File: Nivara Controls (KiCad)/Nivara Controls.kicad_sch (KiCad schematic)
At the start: 11 parts, among them J1 Screw_Terminal_2_P5.00mm, J10 Screw_Terminal_6_P5.00mm, J2 Screw_Terminal_2_P5.00mm, J3 Screw_Terminal_2_P5.00mm, J4 Screw_Terminal_4_P5.00mm, J5 Screw_Terminal_2_P5.00mm, J6 Screw_Terminal_2_P5.00mm, J7 Screw_Terminal_3_P5.00mm, J8 Screw_Terminal_3_P5.00mm, J9 Screw_Terminal_4_P5.00mm

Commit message: Actualization
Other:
- moved on the sheet: J5
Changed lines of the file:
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@@
 	(wire
 		(pts
-			(xy 138.43 142.24) (xy 143.51 142.24)
+			(xy 139.7 142.24) (xy 143.51 142.24)
 		)
 		(stroke
@@
 	(wire
 		(pts
-			(xy 138.43 144.78) (xy 143.51 144.78)
+			(xy 139.7 144.78) (xy 143.51 144.78)
 		)
 		(stroke
@@
 	(symbol
 		(lib_id "PCM_SL_Screw_Terminal:Screw_Terminal_2_P5.00mm")
-		(at 134.62 143.51 180)
+		(at 135.89 143.51 180)
 		(unit 1)
 		(exclude_from_sim no)
@@
 		(dnp no)
 		(property "Reference" "J5"
-			(at 129.794 144.018 0)
+			(at 131.064 144.018 0)
 			(effects
 				(font
@@
 		)
 		(property "Value" "Screw_Terminal_2_P5.00mm"
-			(at 133.985 138.43 0)
+			(at 135.255 138.43 0)
 			(effects
 				(font
@@
 		)
 		(property "Footprint" "TerminalBlock_Phoenix:TerminalBlock_Phoenix_PT-1,5-2-5.0-H_1x02_P5.00mm_Horizontal"
-			(at 133.35 137.16 0)
+			(at 134.62 137.16 0)
 			(effects
 				(font
@@
 		)
 		(property "Datasheet" ""
-			(at 134.62 143.51 0)
+			(at 135.89 143.51 0)
 			(effects
 				(font
@@
 		)
 		(property "Description" ""
-			(at 134.62 143.51 0)
+			(at 135.89 143.51 0)
 			(effects
 				(font
@@
 		)
 		(property "Part Number" ""
-			(at 134.62 143.51 0)
-			(effects
-				(font
+			(at 135.89 143.51 0)
+			(effects
+				(font

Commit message: Actualización
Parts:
- removed J5: Screw_Terminal_2_P5.00mm, TerminalBlock_Phoenix:TerminalBlock_Phoenix_PT-1,5-2-5.0-H_1x02_P5.00mm_Horizontal, symbol PCM_SL_Screw_Terminal:Screw_Terminal_2_P5.00mm
- added J5: Screw_Terminal_4_P5.00mm, TerminalBlock_Phoenix:TerminalBlock_Phoenix_PT-1,5-4-5.0-H_1x04_P5.00mm_Horizontal, symbol PCM_SL_Screw_Terminal:Screw_Terminal_4_P5.00mm
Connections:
- new net Board_NIVARA/+Digit_input_1_+: J5.1
- new net Board_NIVARA/+Digit_input_2_+: J5.3
- new net Board_NIVARA/-Digit_input_1_-: J5.2
- new net Board_NIVARA/-Digit_input_2_-: J5.4
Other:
- sheet Board_NIVARA ports: added +Digit_input_1_+, +Digit_input_2_+, -Digit_input_1_-, -Digit_input_2_-; removed Digit_input_1, Digit_input_2
- moved on the sheet: J1
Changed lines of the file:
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@@
 	(text "24V DC\n"
 		(exclude_from_sim no)
-		(at 124.714 77.978 0)
+		(at 138.684 83.058 0)
 		(effects
 			(font
@@
 	(wire
 		(pts
+			(xy 139.7 140.97) (xy 143.51 140.97)
+		)
+		(stroke
+			(width 0)
+			(type default)
+		)
+	)
+	(wire
+		(pts
 			(xy 201.93 101.6) (xy 205.74 101.6)
 		)
@@
 	(wire
 		(pts
-			(xy 139.7 142.24) (xy 143.51 142.24)
-		)
-		(stroke
-			(width 0)
-			(type default)
-		)
-	)
-	(wire
-		(pts
 			(xy 139.7 120.65) (xy 143.51 120.65)
 		)
@@
 	(wire
 		(pts
+			(xy 139.7 143.51) (xy 143.51 143.51)
+		)
+		(stroke
+			(width 0)
+			(type default)
+		)
+	)
+	(wire
+		(pts
 			(xy 140.97 128.27) (xy 140.97 129.54)
 		)
@@
 	(wire
 		(pts
-			(xy 139.7 144.78) (xy 143.51 144.78)
-		)
-		(stroke
-			(width 0)
-			(type default)
-		)
-	)
-	(wire
-		(pts
 			(xy 139.7 113.03) (xy 143.51 113.03)
 		)
@@
 	(wire
 		(pts
-			(xy 116.84 78.74) (xy 120.65 78.74)
+			(xy 130.81 83.82) (xy 134.62 83.82)
 		)
 		(stroke
@@
 	(wire
 		(pts
-			(xy 120.65 78.74) (xy 120.65 82.55)
+			(xy 134.62 83.82) (xy 134.62 87.63)
+		)
+		(stroke
+			(width 0)
+			(type default)
+		)
+	)
+	(wire
+		(pts
+			(xy 139.7 138.43) (xy 143.51 138.43)
 		)
 		(stroke
@@
 	(wire
 		(pts
+			(xy 139.7 146.05) (xy 143.51 146.05)
+		)
+		(stroke
+			(width 0)
+			(type default)
+		)
+	)
+	(wire
+		(pts
 			(xy 140.97 154.94) (xy 139.7 154.94)
 		)
@@
 	(wire
 		(pts
-			(xy 116.84 76.2) (xy 120.65 76.2)
-		)
-		(stroke
-			(width 0)
-			(type default)
-		)
-	)
-	(wire
-		(pts
-			(xy 120.65 76.2) (xy 120.65 73.66)
+			(xy 130.81 81.28) (xy 134.62 81.28)
+		)
+		(stroke
+			(width 0)
+			(type default)
+		)
+	)
+	(wire
+		(pts
+			(xy 134.62 81.28) (xy 134.62 78.74)
 		)
 		(stroke
@@
 	(symbol
 		(lib_id "power:GND")
-		(at 120.65 82.55 0)
+		(at 134.62 87.63 0)
 		(unit 1)
 		(exclude_from_sim no)
@@
 		(dnp no)
 		(property "Reference" "#PWR01"
-			(at 120.65 88.9 0)
+			(at 134.62 93.98 0)
 			(effects
 				(font
@@
 		)
 		(property "Value" "GND"
-			(at 120.65 86.614 0)
+			(at 134.62 91.694 0)
 			(effects
 				(font
@@
 		)
 		(property "Footprint" ""
-			(at 120.65 82.55 0)
+			(at 134.62 87.63 0)
 			(effects
 				(font
@@
 		)
 		(property "Datasheet" ""
-			(at 120.65 82.55 0)
+			(at 134.62 87.63 0)
 			(effects
 				(font
@@
 		)
 		(property "Description" "Power symbol creates a global label with name \"GND\" , ground"
-			(at 120.65 82.55 0)
+			(at 134.62 87.63 0)
 			(effects
 				(font
@@
 				(path "/42622735-4343-4315-af64-a45701a752b6"
 					(reference "#PWR01")
-					(unit 1)
-				)
-			)
-		)
-	)
-	(symbol
-		(lib_id "PCM_SL_Screw_Terminal:Screw_Terminal_2_P5.00mm")
-		(at 135.89 143.51 180)
-		(unit 1)
-		(exclude_from_sim no)
-		(in_bom yes)
-		(on_board yes)
-		(dnp no)
-		(property "Reference" "J5"
-			(at 131.064 144.018 0)
-			(effects
-				(font
-					(size 1.27 1.27)
-				)
-			)
-		)
-		(property "Value" "Screw_Terminal_2_P5.00mm"
-			(at 135.255 138.43 0)
-			(effects
-				(font
-					(size 1.27 1.27)
-				)
-				(hide yes)
-			)
-		)
-		(property "Footprint" "TerminalBlock_Phoenix:TerminalBlock_Phoenix_PT-1,5-2-5.0-H_1x02_P5.00mm_Horizontal"
-			(at 134.62 137.16 0)
-			(effects
-				(font
-					(size 1.27 1.27)
-				)
-				(hide yes)
-			)
-		)
-		(property "Datasheet" ""
-			(at 135.89 143.51 0)
-			(effects
-				(font
-					(size 1.27 1.27)
-				)
-				(hide yes)
-			)
-		)
-		(property "Description" ""
-			(at 135.89 143.51 0)
-			(effects
-				(font
-					(size 1.27 1.27)
-				)
-				(hide yes)
-			)
-		)
-		(property "Part Number" ""
-			(at 135.89 143.51 0)
-			(effects
-				(font
-					(size 1.27 1.27)
-				)
-			)
-		)
-		(pin "1"
-		)
-		(pin "2"
-		)
-		(instances
-			(project "Nivara Controls"
-				(path "/42622735-4343-4315-af64-a45701a752b6"
-					(reference "J5")
 					(unit 1)
 				)
@@
 	(symbol
 		(lib_id "power:VCC")
-		(at 120.65 73.66 0)
+		(at 134.62 78.74 0)
 		(unit 1)
 		(exclude_from_sim no)
@@
 		(dnp no)
 		(property "Reference" "#PWR02"
-			(at 120.65 77.47 0)
+			(at 134.62 82.55 0)
 			(effects
 				(font
@@
 		)
 		(property "Value" "VCC"
-			(at 120.65 69.85 0)
+			(at 134.62 74.93 0)
 			(effects
 				(font
@@
 		)
 		(property "Footprint" ""
-			(at 120.65 73.66 0)
+			(at 134.62 78.74 0)
 			(effects
 				(font
@@
 		)
 		(property "Datasheet" ""
-			(at 120.65 73.66 0)
+			(at 134.62 78.74 0)
 			(effects
 				(font
@@
 		)
 		(property "Description" "Power symbol creates a global label with name \"VCC\""
-			(at 120.65 73.66 0)
+			(at 134.62 78.74 0)
 			(effects
 				(font
@@
 	)
 	(symbol
+		(lib_id "PCM_SL_Screw_Terminal:Screw_Terminal_4_P5.00mm")
+		(at 135.89 142.24 0)
+		(mirror y)
+		(unit 1)
+		(exclude_from_sim no)
+		(in_bom yes)
+		(on_board yes)
+		(dnp no)
+		(property "Reference" "J5"
+			(at 132.08 140.9699 0)
+			(effects
+				(font
+					(size 1.27 1.27)
+				)
+				(justify left)
+			)
+		)
+		(property "Value" "Screw_Terminal_4_P5.00mm"
+			(at 132.08 143.5099 0)
+			(effects
+				(font
+					(size 1.27 1.27)
+				)
+				(justify left)
+				(hide yes)
+			)
+		)
+		(property "Footprint" "TerminalBlock_Phoenix:TerminalBlock_Phoenix_PT-1,5-4-5.0-H_1x04_P5.00mm_Horizontal"
+			(at 135.89 151.13 0)
+			(effects
+				(font
+					(size 1.27 1.27)
+				)
+				(hide yes)
+			)
+		)
+		(property "Datasheet" ""
+			(at 135.89 139.7 0)
+			(effects
+				(font
+					(size 1.27 1.27)
+				)
+				(hide yes)
+			)
+		)
+		(property "Description" ""
+			(at 135.89 142.24 0)
+			(effects
+				(font
+					(size 1.27 1.27)
+				)
+				(hide yes)
+			)
+		)
+		(property "Part Number" ""
+			(at 135.89 142.24 0)
+			(effects
+				(font
+					(size 1.27 1.27)
+				)
+			)
+		)
+		(pin "3"
+		)
+		(pin "2"
+		)
+		(pin "1"
+		)
+		(pin "4"
+		)
+		(instances
+			(project "Nivara Controls"
+				(path "/42622735-4343-4315-af64-a45701a752b6"
+					(reference "J5")
+					(unit 1)
+				)
+			)
+		)
+	)
+	(symbol
 		(lib_id "PCM_SL_Screw_Terminal:Screw_Terminal_2_P5.00mm")
-		(at 113.03 77.47 180)
+		(at 127 82.55 180)
 		(unit 1)
 		(exclude_from_sim no)
@@
 		(dnp no)
 		(property "Reference" "J1"
-			(at 108.204 77.978 0)
+			(at 122.174 83.058 0)
 			(effects
 				(font
@@
 		)
 		(property "Value" "Screw_Terminal_2_P5.00mm"
-			(at 112.395 72.39 0)
+			(at 126.365 77.47 0)
 			(effects
 				(font
@@
 		)
 		(property "Footprint" "TerminalBlock_Phoenix:TerminalBlock_Phoenix_PT-1,5-2-5.0-H_1x02_P5.00mm_Horizontal"
-			(at 111.76 71.12 0)
+			(at 125.73 76.2 0)
 			(effects
 				(font
@@
 		)
 		(property "Datasheet" ""
-			(at 113.03 77.47 0)
+			(at 127 82.55 0)
 			(effects
 				(font
@@
 		)
 		(property "Description" ""
-			(at 113.03 77.47 0)
+			(at 127 82.55 0)
 			(effects
 				(font
@@
 		)
 		(property "Part Number" ""
-			(at 113.03 77.47 0)
+			(at 127 82.55 0)
 			(effects
 				(font
@@
 			)
 		)
-		(pin "Digit_input_1" input
-			(at 143.51 142.24 180)
-			(effects
-				(font
-					(size 1.27 1.27)
-				)
-				(justify left)
-			)
-		)
-		(pin "Digit_input_2" input
-			(at 143.51 144.78 180)
-			(effects
-				(font
-					(size 1.27 1.27)
-				)
-				(justify left)
-			)
-		)
 		(pin "NPN_input_1" input
 			(at 143.51 100.33 180)
@@
 			)
 		)
+		(pin "+Digit_input_1_+" input
+			(at 143.51 138.43 180)
+			(effects
+				(font
+					(size 1.27 1.27)
+				)
+				(justify left)
+			)
+		)
+		(pin "+Digit_input_2_+" input
+			(at 143.51 143.51 180)
+			(effects
+				(font
+					(size 1.27 1.27)
+				)
+				(justify left)
+			)
+		)
+		(pin "-Digit_input_1_-" input
+			(at 143.51 140.97 180)
+			(effects
+				(font
+					(size 1.27 1.27)
+				)
+				(justify left)
+			)
+		)
+		(pin "-Digit_input_2_-" input
+			(at 143.51 146.05 180)
+			(effects
+				(font
+					(size 1.27 1.27)
+				)
+				(justify left)
+			)
+		)

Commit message: Trabajando en PCB
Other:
- moved on the sheet: J1
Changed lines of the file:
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@@
+	(wire
+		(pts
+			(xy 127 81.28) (xy 134.62 81.28)
+		)
+		(stroke
+			(width 0)
+			(type default)
+		)
+	)
 	(wire
 		(pts
@@
 	(wire
 		(pts
-			(xy 130.81 83.82) (xy 134.62 83.82)
-		)
-		(stroke
-			(width 0)
-			(type default)
-		)
-	)
-	(wire
-		(pts
 			(xy 139.7 123.19) (xy 143.51 123.19)
 		)
@@
 	(wire
 		(pts
-			(xy 130.81 81.28) (xy 134.62 81.28)
-		)
-		(stroke
-			(width 0)
-			(type default)
-		)
-	)
-	(wire
-		(pts
 			(xy 134.62 81.28) (xy 134.62 78.74)
 		)
@@
 		(pts
 			(xy 139.7 125.73) (xy 143.51 125.73)
+		)
+		(stroke
+			(width 0)
+			(type default)
+		)
+	)
+	(wire
+		(pts
+			(xy 127 83.82) (xy 134.62 83.82)
 		)
 		(stroke
@@
 	(symbol
 		(lib_id "PCM_SL_Screw_Terminal:Screw_Terminal_2_P5.00mm")
-		(at 127 82.55 180)
+		(at 123.19 82.55 180)
 		(unit 1)
 		(exclude_from_sim no)
@@
 		(dnp no)
 		(property "Reference" "J1"
-			(at 122.174 83.058 0)
+			(at 118.364 83.058 0)
 			(effects
 				(font
@@
 		)
 		(property "Value" "Screw_Terminal_2_P5.00mm"
-			(at 126.365 77.47 0)
+			(at 122.555 77.47 0)
 			(effects
 				(font
@@
 		)
 		(property "Footprint" "TerminalBlock_Phoenix:TerminalBlock_Phoenix_PT-1,5-2-5.0-H_1x02_P5.00mm_Horizontal"
-			(at 125.73 76.2 0)
-			(effects
-				(font
-					(size 1.27 1.27)
-				)
-				(hide yes)
-			)
-		)
-		(property "Datasheet" ""
-			(at 127 82.55 0)
+			(at 121.92 76.2 0)
+			(effects
+				(font
+					(size 1.27 1.27)
+				)
+				(hide yes)
+			)
+		)
+		(property "Datasheet" ""
+			(at 123.19 82.55 0)
 			(effects
 				(font
@@
 		)
 		(property "Description" ""
-			(at 127 82.55 0)
+			(at 123.19 82.55 0)
 			(effects
 				(font
@@
 		)
 		(property "Part Number" ""
-			(at 127 82.55 0)
-			(effects
-				(font
+			(at 123.19 82.55 0)
+			(effects
+				(font

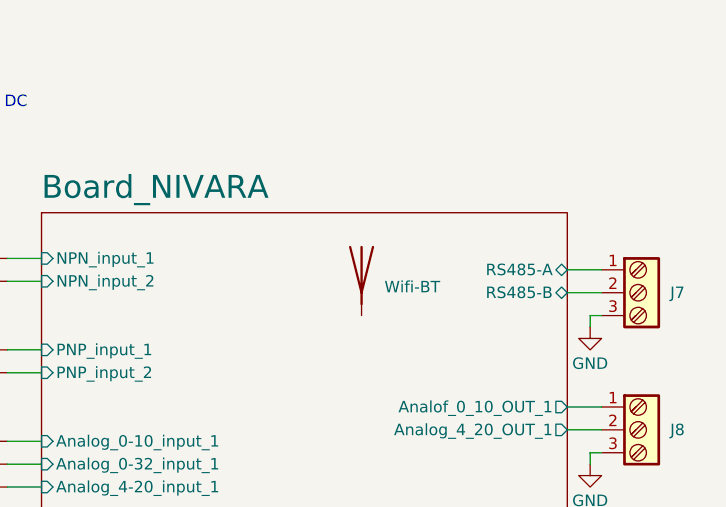
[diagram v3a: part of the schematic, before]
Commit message: Actualizació Orden de componentes
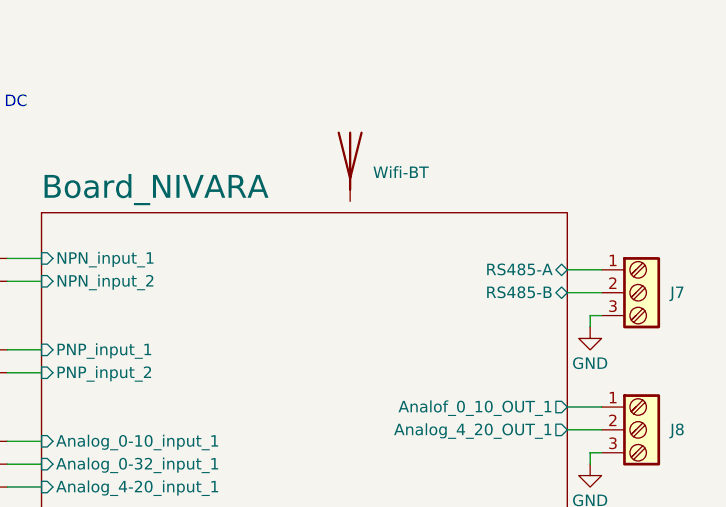
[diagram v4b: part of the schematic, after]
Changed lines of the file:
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@@
 	(symbol
 		(lib_id "Device:Antenna")
-		(at 179.07 101.6 0)
+		(at 177.8 88.9 0)
 		(unit 1)
 		(exclude_from_sim no)
@@
 		(fields_autoplaced yes)
 		(property "Reference" "AE1"
-			(at 181.61 100.9649 0)
+			(at 180.34 88.2649 0)
 			(effects
 				(font
@@
 		)
 		(property "Value" "Wifi-BT"
-			(at 181.61 103.5049 0)
+			(at 180.34 90.8049 0)
 			(effects
 				(font
@@
 		)
 		(property "Footprint" ""
-			(at 179.07 101.6 0)
+			(at 177.8 88.9 0)
 			(effects
 				(font
@@
 		)
 		(property "Datasheet" "~"
-			(at 179.07 101.6 0)
+			(at 177.8 88.9 0)
 			(effects
 				(font
@@
 		)
 		(property "Description" "Antenna"
-			(at 179.07 101.6 0)
+			(at 177.8 88.9 0)
 			(effects
 				(font
@@
 		)
 		(property "Part Number" ""
-			(at 179.07 101.6 0)
+			(at 177.8 88.9 0)
 			(effects
 				(font
